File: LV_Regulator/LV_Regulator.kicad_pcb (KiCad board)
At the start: 4 copper layers, 150 x 100 mm, 195 parts, among them IC1 UCC12040DVE, IC2 MIC29152WU, IC3 MIC29152WU, J1 430450400, J2 430450400, J3 430450800, J4 430450800, J5 SWD, J6 2169890001, K1 41.52.9.005.0010, Q1 BC807, U1 ADM2483xRW, U2 STM32F103C8Tx, U3 25CSM04xxSN, U4 BQ25858QWRRVRQ1, U5 CSD19506KTT, U6 CSD19506KTT, U7 CSD19506KTT, U8 CSD19506KTT, Y1 32.768kHz, Y2 8MHz

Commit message: LV Regulator Switching layout Started
Rough placement of components bigger components, a well as giving a capacitor a 3D model it lacked for the 3D View.
More precise placement is in queue and actual PCB routing.
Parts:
- JP12: footprint Jumper:SolderJumper-3_P1.3mm_Open_Pad1.0x1.5mm -> Jumper:SolderJumper-3_P1.3mm_Open_RoundedPad1.0x1.5mm
- moved C33 359.1 mm to (92.5, 113.2), turned to 90 degrees
- moved C31 358.5 mm to (106.5, 54.7), turned to 90 degrees
- moved C32 358.3 mm to (92.5, 54.5), turned to 90 degrees
- moved J3 347.5 mm to (89.6, 89.3), turned to -90 degrees
- moved C34 345.9 mm to (106.5, 113.2), turned to 90 degrees
- moved R15 325.8 mm to (181.4, -46.0)
- moved R16 325.8 mm to (181.4, -42.7)
- moved R10 324.3 mm to (181.7, -55.4)
- moved R11 324.3 mm to (181.7, -52.1)
- moved D2 321.0 mm to (173.5, -63.7)
- moved D3 321.0 mm to (173.5, -59.1)
- moved D4 321.0 mm to (173.5, -54.5)
- moved D5 321.0 mm to (173.5, -49.9)
- moved IC3 320.2 mm to (143.6, 64.5), turned to 180 degrees
- moved F3 318.4 mm to (155.9, -63.7)
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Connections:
- net +3.3V renamed VBAT
- TP3 pad 1: unconnected-(TP3-Pad1) -> VOUT
- TP39 pad 1: unconnected-(TP39-Pad1) -> GND
- TP40 pad 1: unconnected-(TP40-Pad1) -> GND
- TP41 pad 1: unconnected-(TP41-Pad1) -> GND
- TP42 pad 1: unconnected-(TP42-Pad1) -> GND
- TP43 pad 1: unconnected-(TP43-Pad1) -> GND
- TP44 pad 1: unconnected-(TP44-Pad1) -> GND

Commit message: Update LV_Regulator.kicad_pcb
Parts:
- C26, C27, C28, C29, C30, C37, D6, D7, D8, D9, JP10, JP11, JP12, JP13, L1, R28, R29, R30, R31, R32, R33, R34, R35, R36, R37, R38, R39, R40, R41, R42, R43, R44, R45, R46, R47, R48, R49, R53, R54, U4: moved to B.Cu
- moved R38 132.1 mm to (100.6, 100.1)
- moved R28 130.7 mm to (100.5, 90.5)
- moved R29 130.4 mm to (100.5, 93.5), turned to 180 degrees
- moved R31 127.9 mm to (100.5, 97.6)
- moved R30 119.2 mm to (100.5, 85.1)
- moved R37 118.9 mm to (100.5, 82.6)
- moved R35 109.9 mm to (115.5, 71.5)
- moved R39 107.3 mm to (100.7, 76.7)
- moved R36 105.5 mm to (120.5, 71.5)
- moved R40 102.3 mm to (105.7, 76.7)
- moved R32 100.2 mm to (100.5, 71.5)
- moved R41 97.4 mm to (110.7, 76.7)
- moved R33 95.3 mm to (105.5, 71.5)
- moved R34 90.6 mm to (110.5, 71.5)
- moved JP11 83.3 mm to (96.5, 83.8)
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
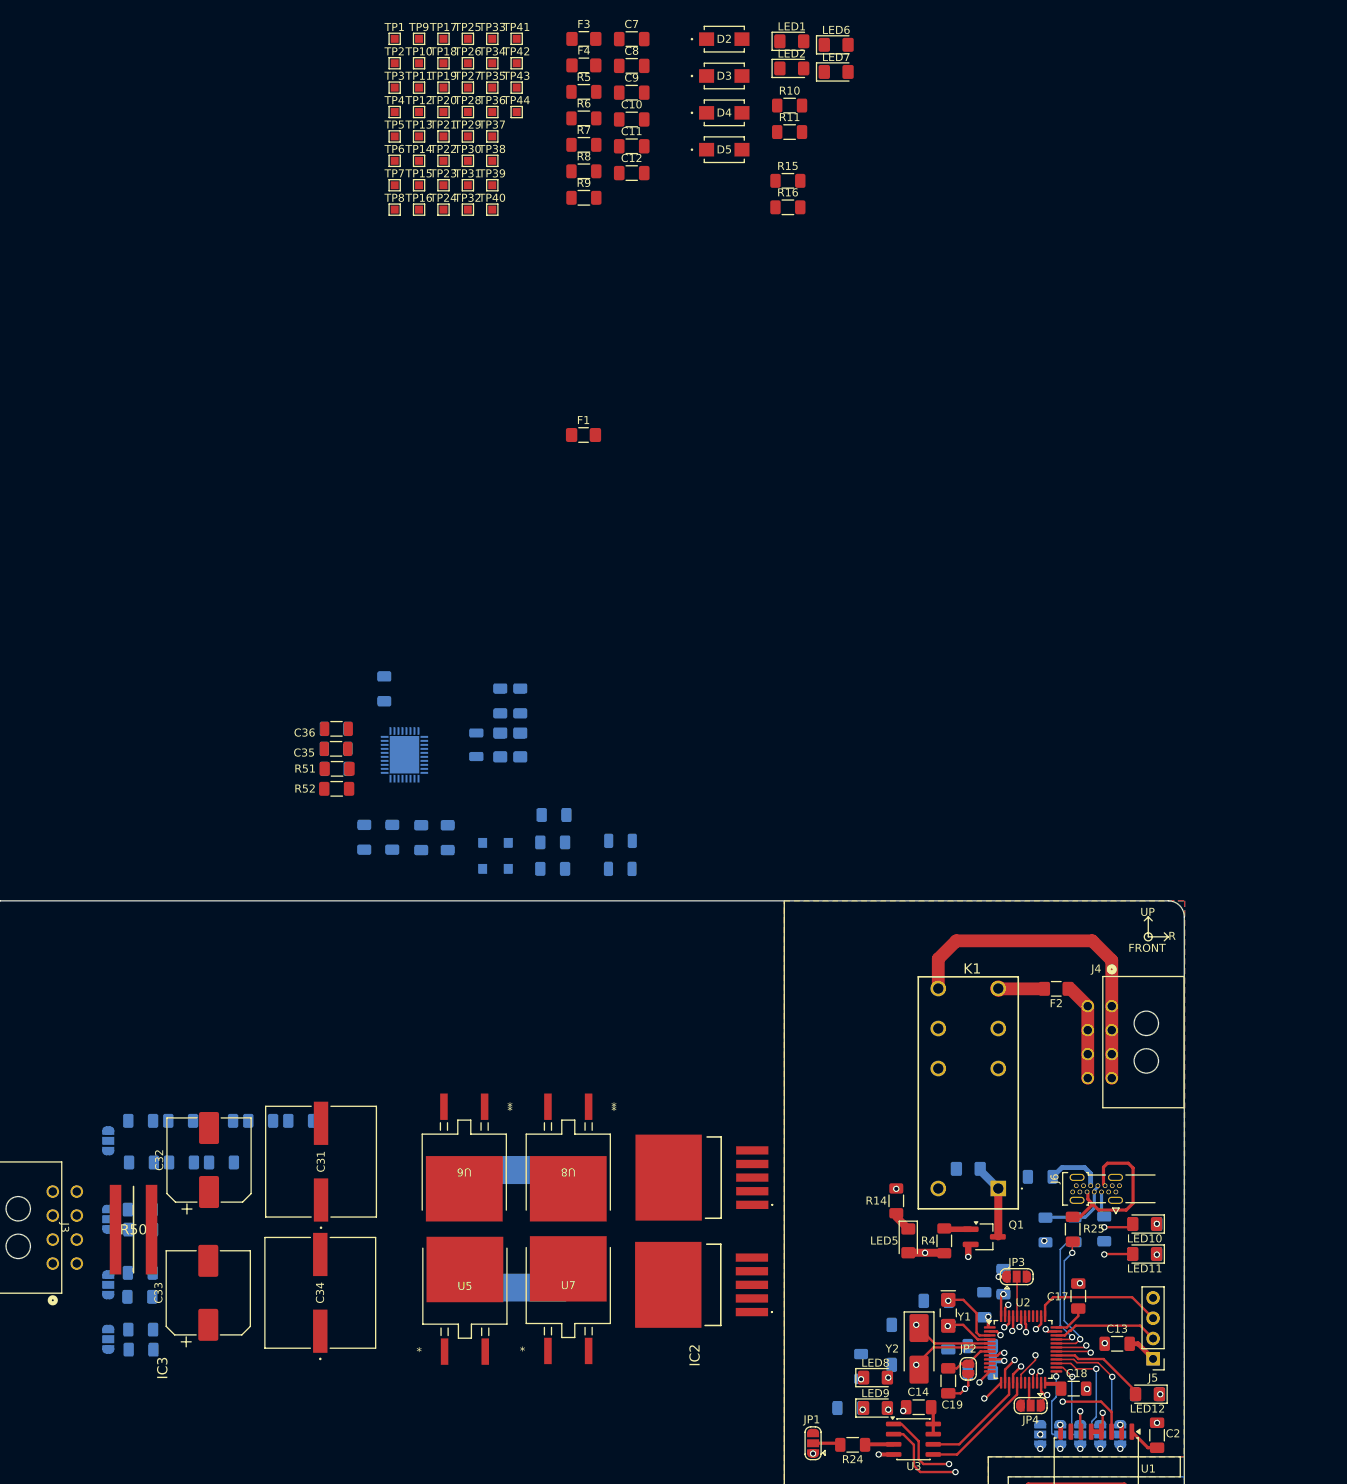
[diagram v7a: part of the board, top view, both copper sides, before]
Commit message: Component Placement and Routing
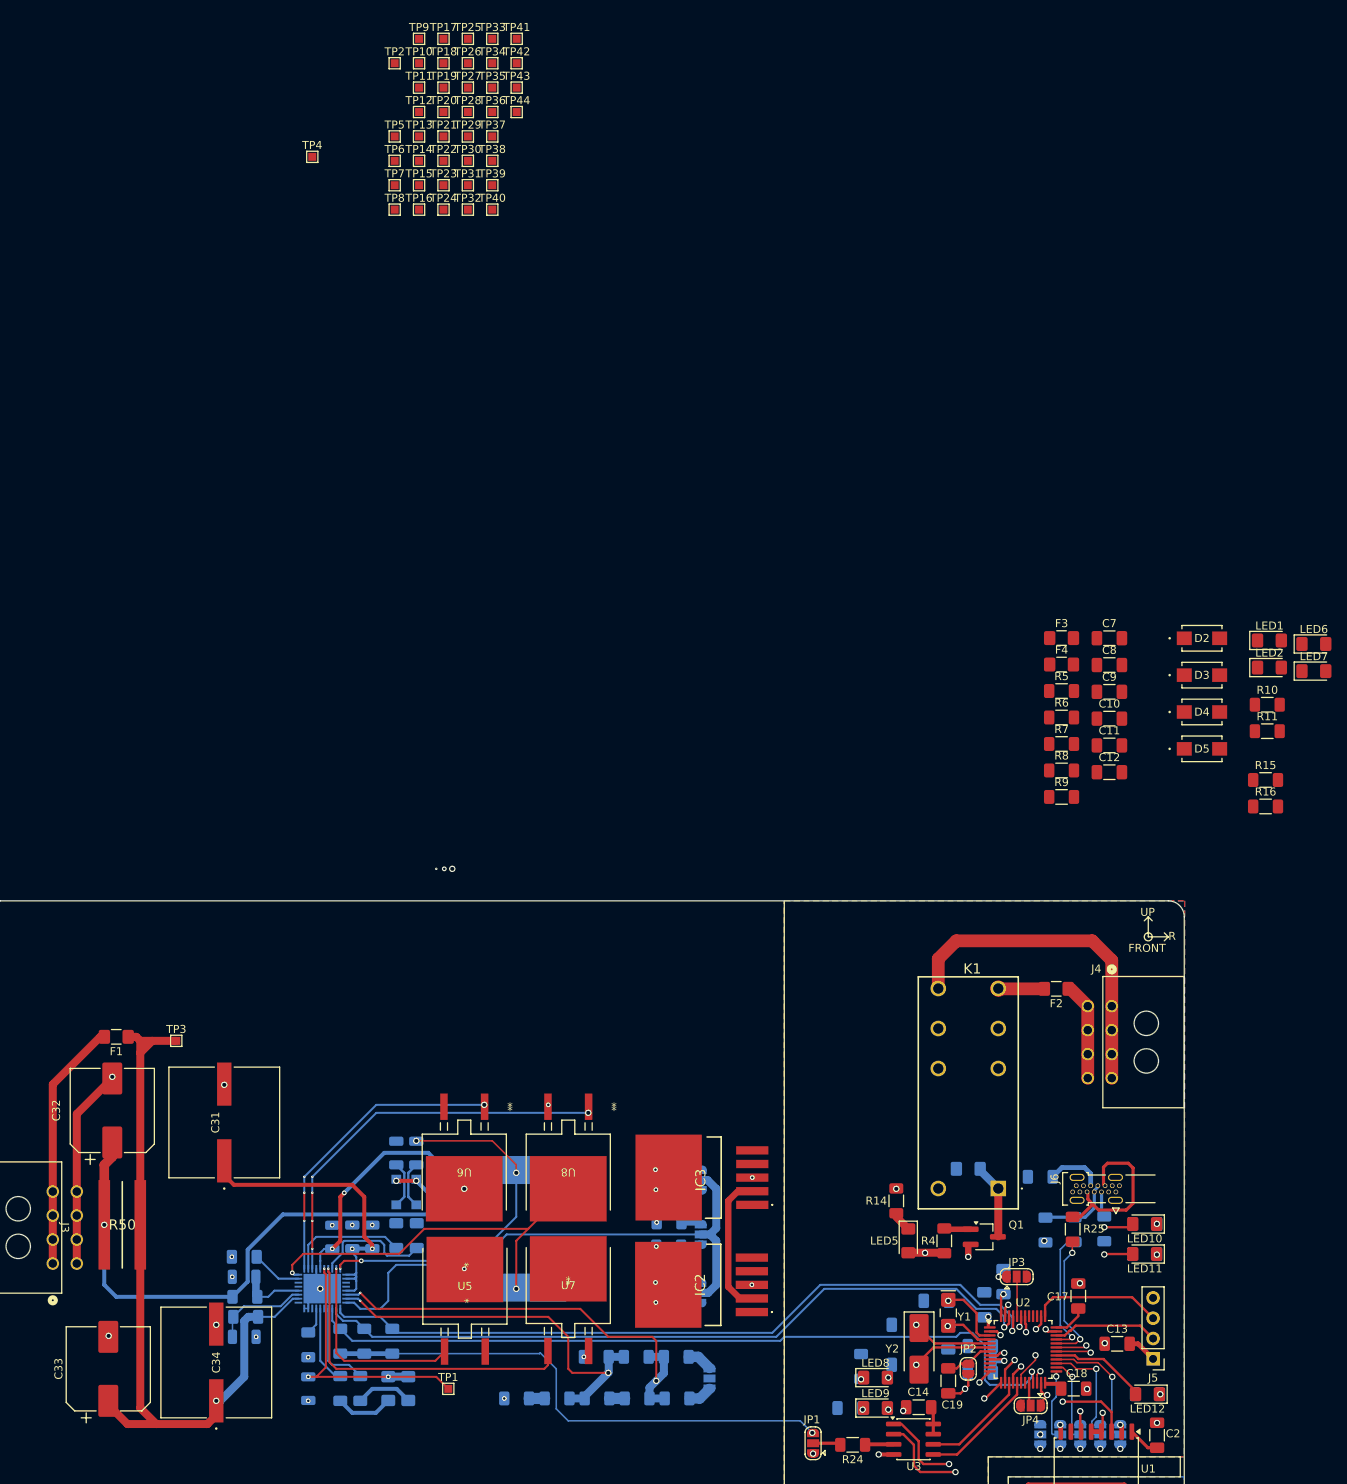
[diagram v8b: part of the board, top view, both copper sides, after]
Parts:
- C35, C36, R51, R52: moved to B.Cu
- TP1: value TestPoint -> REGN TP
- TP3: value TestPoint -> V_OUT TP
- moved TP1 168.9 mm to (139.0, 105.0)
- moved TP3 122.2 mm to (105.0, 61.5)
- moved C10 95.8 mm to (221.6, 21.2)
- moved C11 95.8 mm to (221.6, 24.6)
- moved C12 95.8 mm to (221.6, 27.9)
- moved C9 95.8 mm to (221.6, 17.9)
- moved D2 95.8 mm to (233.2, 11.2)
- moved D3 95.8 mm to (233.2, 15.8)
- moved D4 95.8 mm to (233.2, 20.4)
- moved D5 95.8 mm to (233.2, 25.0)
- moved F3 95.8 mm to (215.7, 11.2)
- moved F4 95.8 mm to (215.7, 14.5)
- moved LED1 95.8 mm to (241.6, 11.5)
- moved LED2 95.8 mm to (241.6, 14.8)
- moved LED6 95.8 mm to (247.2, 11.9)
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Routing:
- net INT_N: track 1.44 -> 98.8 mm
- net VOUT: track 0.00 -> 94.0 mm, vias 0 -> 1
- net I2C_SCL: track 1.89 -> 93.4 mm
- net I2C_SDA: track 1.71 -> 92.9 mm
- net Net-(U6-D): track 0.00 -> 72.1 mm, vias 0 -> 2
- net Izbor_frekvencije: track 0.00 -> 69.2 mm
- net VBAT: track 27.5 -> 93.7 mm, vias 9 -> 10
- net SYS: track 0.00 -> 57.0 mm, vias 0 -> 3
- net ACUV: track 0.00 -> 56.1 mm, vias 0 -> 2
- net LODRV2_FET3: track 0.00 -> 49.3 mm, vias 0 -> 5
- net ACOV: track 0.00 -> 49.2 mm, vias 0 -> 2
- net SW2: track 0.00 -> 48.4 mm, vias 0 -> 2
- net SW1: track 0.00 -> 45.2 mm, vias 0 -> 4
- net LODRV1_FET2: track 0.00 -> 41.3 mm, vias 0 -> 1
- net HIDRV2_FET4: track 0.00 -> 37.7 mm, vias 0 -> 4
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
